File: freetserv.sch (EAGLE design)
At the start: 72 parts, among them IC2 SN75240PW, Q1 12MHz, Q2 6MHz, U1 MCP16311-E/MS

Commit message: wire up a serial port
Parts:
- removed SL1: (no value), con-lstb:MA05-1
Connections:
- removed net N$25: DRV0A.DOUT1, SL1.2
- removed net N$8: DRV0A.DOUT2, SL1.4
- new net N$37: DRV0A.DOUT1
- net GND: no longer SL1.5
- net N$19: no longer SL1.1
- net N$9: no longer SL1.3
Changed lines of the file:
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@@
 <attribute name="PARTNO" value="1276-1003-1-ND"/>
 </part>
-<part name="SL1" library="con-lstb" deviceset="MA05-1" device=""/>
 <part name="C17" library="resistor" deviceset="C-EU" device="C0805" value="0.1uF">
 <attribute name="PARTNO" value="1276-1003-1-ND"/>
@@
 <attribute name="PARTNO" value="490-10517-1-ND"/>
 </part>
-<part name="GND11" library="supply1" deviceset="GND" device=""/>
 <part name="DRV0B" library="Texas Instruments_By_element14_Batch_1" deviceset="MAX3232ECPW" device="">
 <attribute name="PARTNO" value="296-19263-1-ND"/>
@@
 <attribute name="PARTNO" value="311-27.0CRCT-ND"/>
 </part>
+<part name="GND11" library="supply1" deviceset="GND" device=""/>
+<part name="GND57" library="supply1" deviceset="GND" device=""/>
 </parts>
 <sheets>
@@
 <attribute name="PARTNO" x="134.62" y="86.36" size="1.778" layer="96" display="off"/>
 </instance>
-<instance part="SL1" gate="G$1" x="195.58" y="104.14" rot="R180"/>
 <instance part="C17" gate="G$1" x="137.16" y="114.3" rot="R90">
 <attribute name="PARTNO" x="137.16" y="114.3" size="1.778" layer="96" display="off"/>
@@
 <instance part="GND2" gate="1" x="-45.72" y="350.52"/>
 <instance part="GND3" gate="1" x="-63.5" y="322.58" rot="R90"/>
-<instance part="U$1" gate="G$1" x="-55.88" y="-73.66">
-<attribute name="PARTNO" x="-55.88" y="-73.66" size="1.778" layer="96" display="off"/>
+<instance part="U$1" gate="G$1" x="251.46" y="266.7" rot="R270">
+<attribute name="PARTNO" x="251.46" y="266.7" size="1.778" layer="96" rot="R270" display="off"/>
 </instance>
 <instance part="U1" gate="G$1" x="2.54" y="330.2">
@@
 <attribute name="PARTNO" x="66.04" y="330.2" size="1.778" layer="96" display="off"/>
 </instance>
-<instance part="GND11" gate="1" x="187.96" y="96.52"/>
 <instance part="DRV0B" gate="A" x="269.24" y="71.12">
 <attribute name="PARTNO" x="269.24" y="71.12" size="1.778" layer="96" display="off"/>
@@
 <attribute name="PARTNO" x="88.9" y="261.62" size="1.778" layer="96" display="off"/>
 </instance>
+<instance part="GND11" gate="1" x="243.84" y="129.54" rot="R270"/>
+<instance part="GND57" gate="1" x="243.84" y="127" rot="R270"/>
 </instances>
 <busses>
@@
 </segment>
 <segment>
-<pinref part="SL1" gate="G$1" pin="5"/>
-<pinref part="GND11" gate="1" pin="GND"/>
-</segment>
-<segment>
 <pinref part="DRV0B" gate="A" pin="GND"/>
 <pinref part="GND12" gate="1" pin="GND"/>
@@
 <wire x1="142.24" y1="109.22" x2="129.54" y2="109.22" width="0.1524" layer="91"/>
 <wire x1="129.54" y1="109.22" x2="129.54" y2="124.46" width="0.1524" layer="91"/>
-<wire x1="129.54" y1="124.46" x2="187.96" y2="124.46" width="0.1524" layer="91"/>
-<pinref part="SL1" gate="G$1" pin="1"/>
-<wire x1="187.96" y1="124.46" x2="187.96" y2="109.22" width="0.1524" layer="91"/>
+<wire x1="129.54" y1="124.46" x2="198.12" y2="124.46" width="0.1524" layer="91"/>
+<wire x1="198.12" y1="124.46" x2="198.12" y2="132.08" width="0.1524" layer="91"/>
+<wire x1="198.12" y1="132.08" x2="246.38" y2="132.08" width="0.1524" layer="91"/>
 </segment>
 </net>
@@
 </segment>
 </net>
-<net name="N$8" class="0">
-<segment>
-<pinref part="DRV0A" gate="A" pin="DOUT2"/>
-<wire x1="177.8" y1="104.14" x2="182.88" y2="106.68" width="0.1524" layer="91"/>
-<wire x1="182.88" y1="106.68" x2="182.88" y2="101.6" width="0.1524" layer="91"/>
-<pinref part="SL1" gate="G$1" pin="4"/>
-<wire x1="182.88" y1="101.6" x2="187.96" y2="101.6" width="0.1524" layer="91"/>
-</segment>
-</net>
 <net name="N$9" class="0">
 <segment>
@@
 <wire x1="124.46" y1="106.68" x2="116.84" y2="106.68" width="0.1524" layer="91"/>
 <wire x1="116.84" y1="106.68" x2="116.84" y2="127" width="0.1524" layer="91"/>
-<wire x1="116.84" y1="127" x2="203.2" y2="127" width="0.1524" layer="91"/>
-<wire x1="203.2" y1="127" x2="203.2" y2="88.9" width="0.1524" layer="91"/>
-<wire x1="203.2" y1="88.9" x2="177.8" y2="88.9" width="0.1524" layer="91"/>
-<wire x1="177.8" y1="88.9" x2="177.8" y2="104.14" width="0.1524" layer="91"/>
-<pinref part="SL1" gate="G$1" pin="3"/>
-<wire x1="187.96" y1="104.14" x2="177.8" y2="104.14" width="0.1524" layer="91"/>
+<wire x1="246.38" y1="137.16" x2="193.04" y2="137.16" width="0.1524" layer="91"/>
+<wire x1="193.04" y1="137.16" x2="193.04" y2="127" width="0.1524" layer="91"/>
+<wire x1="193.04" y1="127" x2="116.84" y2="127" width="0.1524" layer="91"/>
 </segment>
 </net>
@@
 <wire x1="119.38" y1="10.16" x2="119.38" y2="-20.32" width="0.1524" layer="91"/>
 <wire x1="119.38" y1="-20.32" x2="393.7" y2="-20.32" width="0.1524" layer="91"/>
-</segment>
-</net>
-<net name="N$25" class="0">
-<segment>
-<pinref part="SL1" gate="G$1" pin="2"/>
-<wire x1="187.96" y1="106.68" x2="185.42" y2="106.68" width="0.1524" layer="91"/>
-<wire x1="185.42" y1="106.68" x2="185.42" y2="109.22" width="0.1524" layer="91"/>
-<pinref part="DRV0A" gate="A" pin="DOUT1"/>
-<wire x1="185.42" y1="109.22" x2="177.8" y2="114.3" width="0.1524" layer="91"/>
 </segment>
 </net>
@@
 </segment>
 </net>
+<net name="N$8" class="0">
+<segment>
+<wire x1="246.38" y1="119.38" x2="210.82" y2="119.38" width="0.1524" layer="91"/>
+<wire x1="210.82" y1="119.38" x2="210.82" y2="104.14" width="0.1524" layer="91"/>
+<wire x1="210.82" y1="104.14" x2="177.8" y2="104.14" width="0.1524" layer="91"/>
+</segment>
+</net>
+<net name="N$37" class="0">
+<segment>
+<wire x1="246.38" y1="124.46" x2="203.2" y2="124.46" width="0.1524" layer="91"/>
+<wire x1="203.2" y1="124.46" x2="203.2" y2="114.3" width="0.1524" layer="91"/>
+<pinref part="DRV0A" gate="A" pin="DOUT1"/>
+<wire x1="203.2" y1="114.3" x2="177.8" y2="114.3" width="0.1524" layer="91"/>
+</segment>
+</net>

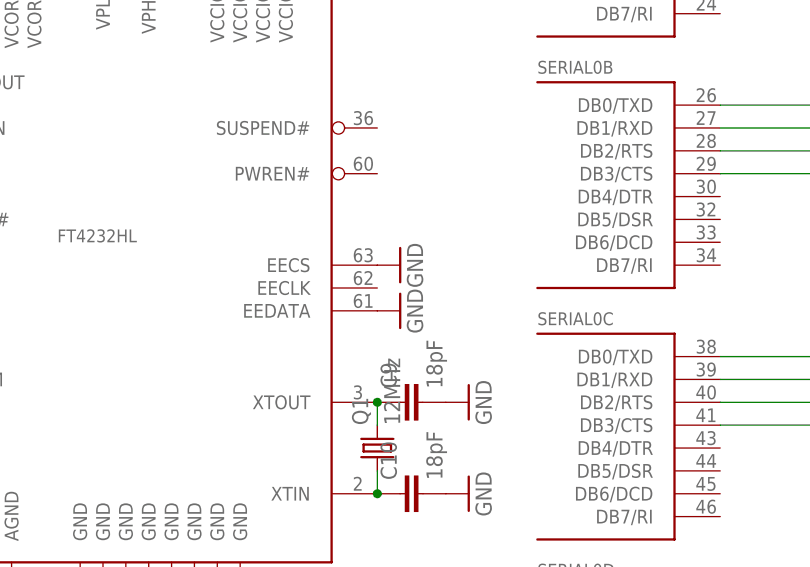
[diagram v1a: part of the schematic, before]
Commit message: Bugfix: disconnect EEDATA/EECS from GND (Thanks Volker!)
With this fix, the FTDI converter is recognized by the host \o/
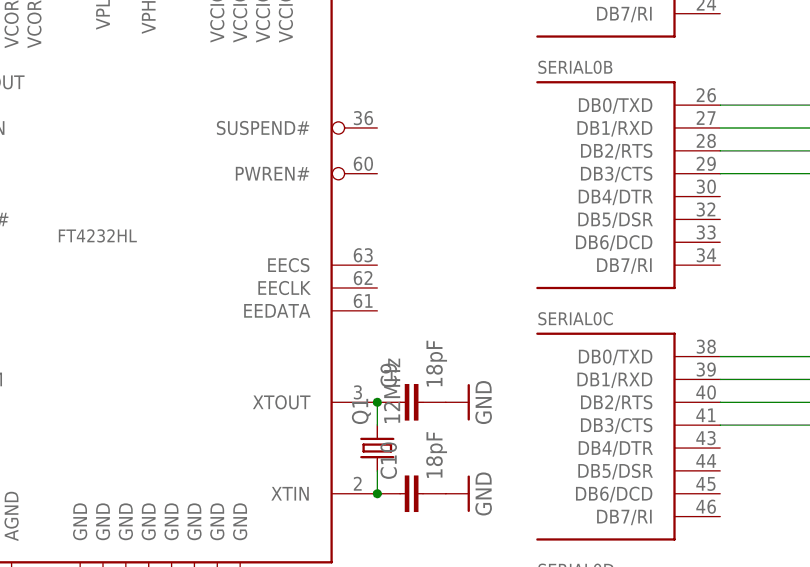
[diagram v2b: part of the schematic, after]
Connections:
- net GND: no longer SERIAL0CORE.EECS, SERIAL0CORE.EEDATA
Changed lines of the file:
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@@
 <?xml version="1.0" encoding="utf-8"?>
 <!DOCTYPE eagle SYSTEM "eagle.dtd">
-<eagle version="7.3.0">
+<eagle version="7.4.0">
 <drawing>
 <settings>
@@
 <part name="GND17" library="supply1" deviceset="GND" device=""/>
 <part name="GND18" library="supply1" deviceset="GND" device=""/>
-<part name="GND19" library="supply1" deviceset="GND" device=""/>
-<part name="GND20" library="supply1" deviceset="GND" device=""/>
 <part name="FERRITE1" library="Wurth_Elektronik_Passive_rev15d" deviceset="WE-KI" device="_0805A" value="330">
 <attribute name="PARTNO" value="490-5988-1-ND"/>
@@
 <instance part="GND17" gate="1" x="71.12" y="40.64" rot="R90"/>
 <instance part="GND18" gate="1" x="71.12" y="30.48" rot="R90"/>
-<instance part="GND19" gate="1" x="63.5" y="55.88" rot="R90"/>
-<instance part="GND20" gate="1" x="63.5" y="50.8" rot="R90"/>
 <instance part="FERRITE1" gate="G$1" x="35.56" y="116.84" rot="R270">
 <attribute name="PARTNO" x="35.56" y="116.84" size="1.778" layer="96" display="off"/>
@@
 </segment>
 <segment>
-<pinref part="SERIAL0" gate="CORE" pin="EECS"/>
-<pinref part="GND19" gate="1" pin="GND"/>
-</segment>
-<segment>
-<pinref part="SERIAL0" gate="CORE" pin="EEDATA"/>
-<pinref part="GND20" gate="1" pin="GND"/>
-</segment>
-<segment>

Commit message: Volker re-organized the schematics
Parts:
- removed DRV0A, DRV0B, DRV0C, DRV0D: MAX3232ECPW, Texas Instruments_By_element14_Batch_1:MAX3232ECPW
- removed FERRITE1, FERRITE2: 330, Wurth_Elektronik_Passive_rev15d:WE-KI_0805A
- removed HUB0: TUSB2046BVF, Texas Instruments_By_element14_Batch_1:TUSB2046BVF
- removed SERIAL0: FT4232HL, ftdichip-6:FT4232HL
- removed U1: MCP16311-E/MS, microchip:MCP16311-E/MS
- added C46: 0.1uF, resistor:C-EUC0805
- added FB1, FB2\: 330, Wurth_Elektronik_Passive_rev15d:WE-KI_0805A
- added IC1: MCP16311-E/MS, microchip:MCP16311-E/MS
- added IC3: TUSB2046BVF, Texas Instruments_By_element14_Batch_1:TUSB2046BVF
- added IC4: FT4232HL, ftdichip-6:FT4232HL
- added IC5, IC6, IC7, IC8: MAX3232ECPW, Texas Instruments_By_element14_Batch_1:MAX3232ECPW
- added R10, R9: 27, resistor:R-EU_R0805
- added R11, R12: 10k, resistor:R-EU_R0805
- added SL1, SL2, SL3, SL4: (no value), con-lstb:MA05-1
- R2: value 12K -> 12K / 1%
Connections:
- net N$12 renamed DX0_N
- net N$13 renamed DX0_P
- removed net N$19: DRV0A.RIN1
- removed net N$20: C1.1, DRV0B.C1-
- removed net N$23: DRV0B.DIN1, SERIAL0B.DB0/TXD
- removed net N$24: DRV0B.ROUT1, SERIAL0B.DB1/RXD
- removed net N$26: C23.2, DRV0B.V+
- removed net N$35: DRV0A.DIN1, SERIAL0A.DB0/TXD
- removed net N$36: DRV0A.ROUT1, SERIAL0A.DB1/RXD
- removed net N$38: C24.2, DRV0B.V-
- removed net N$41: IC2.D, R6.2, R8.2
- removed net N$43: C37.2, HUB0.~RESET, R7.1, SERIAL0CORE.RESET#
- removed net N$5: DRV0A.DIN2, SERIAL0A.DB2/RTS
- removed net N$51: C26.2, DRV0C.C1+
- removed net N$54: C27.1, DRV0C.C2-
- removed net N$55: DRV0C.DIN1, SERIAL0C.DB0/TXD
- removed net N$56: DRV0C.ROUT1, SERIAL0C.DB1/RXD
- removed net N$58: C28.2, DRV0C.V+
- removed net N$59: C29.2, DRV0C.V-
- removed net N$65: C31.2, DRV0D.C1+
- removed net N$68: C32.1, DRV0D.C2-
- removed net N$69: DRV0D.DIN1, SERIAL0D.DB0/TXD
- removed net N$7: DRV0A.ROUT2, SERIAL0A.DB3/CTS
- removed net N$70: DRV0D.ROUT1, SERIAL0D.DB1/RXD
- removed net N$72: C33.2, DRV0D.V+
- removed net N$73: C34.2, DRV0D.V-
- removed net N$75: DRV0D.DIN2, SERIAL0D.DB2/RTS
- removed net N$76: DRV0D.ROUT2, SERIAL0D.DB3/CTS
- removed net N$9: DRV0A.RIN2
- removed net USB0_D2_N: HUB0.DM2, SERIAL0CORE.USBDM
- removed net USB0_D2_P: HUB0.DP2, SERIAL0CORE.USBDP
- removed net USB0_DM_N: HUB0.DM0, IC2.C, R1.2
- removed net USB0_DM_P: HUB0.DP0, R6.1
- new net !OVRCUR1: IC3.~OVRCUR1, R11.2
- new net !OVRCUR2: IC3.~OVRCUR2, R12.2
- new net !OVRCUR3: IC3.~OVRCUR3
- new net !OVRCUR4: IC3.~OVRCUR4
- new net !PWRON1: IC3.~PWRON1
- new net !PWRON2: IC3.~PWRON2
- new net !PWRON3: IC3.~PWRON3
- new net !PWRON4: IC3.~PWRON4
- new net !RESET: C37.2, IC3.~RESET, IC4CORE.RESET#, R7.1
- new net CTS1E: IC5.RIN2, SL1.3
- new net CTS1I: IC4A.DB3/CTS, IC5.ROUT2
- new net CTS2E: IC6.RIN2, SL2.3
- new net CTS2I: IC4B.DB3/CTS, IC6.ROUT2
- new net CTS3E: IC7.RIN2, SL3.3
- new net CTS3I: IC4C.DB3/CTS, IC7.ROUT2
- new net CTS4E: IC8.RIN2, SL4.3
- new net CTS4I: IC4D.DB3/CTS, IC8.ROUT2
- new net D0_N: IC2.B, IC3.DM0, R1.2
- new net D0_P: IC2.A, IC3.DP0, R6.2, R8.2
- new net D1_N: IC2.D, IC3.DM1, R9.2
- new net D1_P: IC2.C, IC3.DP1, R10.2
- new net D2_N: IC3.DM2, IC4CORE.USBDM
- new net D2_P: IC3.DP2, IC4CORE.USBDP
- new net D3_N: IC3.DM3
- new net D3_P: IC3.DP3
- new net D4_N: IC3.DM4
- new net D4_P: IC3.DP4
- new net DX1_N: R9.1, USB_IN.D-
- new net DX1_P: R10.1, USB_IN.D+
- new net N$12: C22.1, IC6.C2-
- new net N$49: C27.1, IC7.C2-
- new net N$60: C31.2, IC8.C1+
- new net N$63: C32.1, IC8.C2-
- new net RTS1E: IC5.DOUT2, SL1.4
- new net RTS1I: IC4A.DB2/RTS, IC5.DIN2
- new net RTS2E: IC6.DOUT2, SL2.4
- new net RTS2I: IC4B.DB2/RTS, IC6.DIN2
- new net RTS3E: IC7.DOUT2, SL3.4
- new net RTS3I: IC4C.DB2/RTS, IC7.DIN2
- new net RTS4E: IC8.DOUT2, SL4.4
- new net RTS4I: IC4D.DB2/RTS, IC8.DIN2
- new net RXD1E: IC5.RIN1, SL1.1
- new net RXD1I: IC4A.DB1/RXD, IC5.ROUT1
- new net RXD2E: IC6.RIN1, SL2.1
- new net RXD2I: IC4B.DB1/RXD, IC6.ROUT1
- new net RXD3E: IC7.RIN1, SL3.1
- new net RXD3I: IC4C.DB1/RXD, IC7.ROUT1
- new net RXD4E: IC8.RIN1, SL4.1
- new net RXD4I: IC4D.DB1/RXD, IC8.ROUT1
- new net TXD1E: IC5.DOUT1, SL1.2
- new net TXD1I: IC4A.DB0/TXD, IC5.DIN1
- new net TXD2E: IC6.DOUT1, SL2.2
- new net TXD2I: IC4B.DB0/TXD, IC6.DIN1
- new net TXD3E: IC7.DOUT1, SL3.2
- new net TXD3I: IC4C.DB0/TXD, IC7.DIN1
- new net TXD4E: IC8.DOUT1, SL4.2
- new net TXD4I: IC4D.DB0/TXD, IC8.DIN1
- net +1V8: now also IC4CORE.VCORE@1, IC4CORE.VCORE@2, IC4CORE.VCORE@3, IC4CORE.VREGOUT; no longer SERIAL0CORE.VCORE@1, SERIAL0CORE.VCORE@2, SERIAL0CORE.VCORE@3, SERIAL0CORE.VREGOUT
- net +3V3: now also C46.2, FB1.1, FB2\.1, IC3.VCC, IC3.~EXTMEM, IC4CORE.VCCIO@1, IC4CORE.VCCIO@2, IC4CORE.VCCIO@3, IC4CORE.VCCIO@4, IC4CORE.VREGIN, IC5.VCC, IC6.VCC, IC7.VCC, IC8.VCC, R11.1, R12.1, R6.1; no longer DRV0A.VCC, DRV0B.VCC, DRV0C.VCC, DRV0D.VCC, FERRITE1.1, FERRITE2.1, HUB0.VCC, HUB0.VCC_2, HUB0.~EXTMEM, HUB0.~OVRCUR1, HUB0.~OVRCUR2, HUB0.~OVRCUR3, HUB0.~OVRCUR4, SERIAL0CORE.VCCIO@1, SERIAL0CORE.VCCIO@2, SERIAL0CORE.VCCIO@3, SERIAL0CORE.VCCIO@4, SERIAL0CORE.VREGIN
- net +5V: now also IC1.EN, IC1.VIN; no longer U1.EN, U1.VIN
- net GND: now also C46.1, IC1.AGND, IC1.GND, IC3.BUSPWR, IC3.GND, IC3.TSTMODE, IC3.TSTPLL/48MCLK, IC4CORE.AGND, IC4CORE.GND@1, IC4CORE.GND@2, IC4CORE.GND@3, IC4CORE.GND@4, IC4CORE.GND@5, IC4CORE.GND@6, IC4CORE.GND@7, IC4CORE.GND@8, IC4CORE.TEST, IC5.GND, IC6.GND, IC7.GND, IC8.GND, SL1.5, SL2.5, SL3.5, SL4.5; no longer DRV0A.GND, DRV0B.GND, DRV0C.GND, DRV0D.GND, HUB0.BUSPWR, HUB0.EEDATA/GANGED, HUB0.GND, HUB0.GND_2, HUB0.TSTMODE, HUB0.TSTPLL/48MCLK, SERIAL0CORE.AGND, SERIAL0CORE.GND@1, SERIAL0CORE.GND@2, SERIAL0CORE.GND@3, SERIAL0CORE.GND@4, SERIAL0CORE.GND@5, SERIAL0CORE.GND@6, SERIAL0CORE.GND@7, SERIAL0CORE.GND@8, SERIAL0CORE.TEST, U1.AGND, U1.GND
- net N$1: now also C1.2, IC6.C1+; no longer HUB0.DP1, IC2.B, USB_IN.D+
- net N$10: now also IC1.VCC; no longer U1.VCC
- net N$11: now also C22.2, IC6.C2+; no longer C1.2, DRV0B.C1+
- net N$14: now also IC4CORE.REF; no longer SERIAL0CORE.REF
- net N$15: now also IC4CORE.XTOUT; no longer SERIAL0CORE.XTOUT
- net N$16: now also IC4CORE.XTIN; no longer SERIAL0CORE.XTIN
- net N$17: now also FB2\.2, IC4CORE.VPHY; no longer FERRITE1.2, SERIAL0CORE.VPHY
- net N$18: now also FB1.2, IC4CORE.VPLL; no longer FERRITE2.2, SERIAL0CORE.VPLL
- net N$2: now also C1.1, IC6.C1-; no longer HUB0.DM1, IC2.A, USB_IN.D-
- net N$21: now also C23.2, IC6.V+; no longer C22.2, DRV0B.C2+
- net N$22: now also C24.2, IC6.V-; no longer C22.1, DRV0B.C2-
- net N$3: now also IC1.BOOST; no longer U1.BOOST
- net N$31: now also IC5.C1+; no longer DRV0A.C1+
- net N$32: now also IC5.C1-; no longer DRV0A.C1-
- net N$33: now also IC5.C2+; no longer DRV0A.C2+
- net N$34: now also IC5.C2-; no longer DRV0A.C2-
- net N$37: now also IC3.XTAL2, R3.1; no longer DRV0A.DOUT1
- net N$39: now also IC5.V+; no longer DRV0A.V+
- net N$4: now also IC1.SW; no longer U1.SW
- net N$40: now also IC5.V-; no longer DRV0A.V-
- net N$44: now also IC3.XTAL1; no longer HUB0.XTAL1
- net N$46: now also C26.2, IC7.C1+; no longer HUB0.XTAL2, R3.1
- net N$47: now also C26.1, IC7.C1-; no longer DRV0B.DIN2, SERIAL0B.DB2/RTS
- net N$48: now also C27.2, IC7.C2+; no longer DRV0B.ROUT2, SERIAL0B.DB3/CTS
- net N$52: now also C28.2, IC7.V+; no longer C26.1, DRV0C.C1-
- net N$53: now also C29.2, IC7.V-; no longer C27.2, DRV0C.C2+
- net N$6: now also IC1.VFB; no longer U1.VFB
- net N$61: now also C31.1, IC8.C1-; no longer DRV0C.DIN2, SERIAL0C.DB2/RTS
- net N$62: now also C32.2, IC8.C2+; no longer DRV0C.ROUT2, SERIAL0C.DB3/CTS
- net N$66: now also C33.2, IC8.V+; no longer C31.1, DRV0D.C1-
- net N$67: now also C34.2, IC8.V-; no longer C32.2, DRV0D.C2+
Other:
- note added: "(GPIO, SCT, ADC)"
- note added: "(I2C0)"
- note added: "(I2C1)"
- note added: "(I2C1, 3V3 analog)"
- note added: "(SSP0, 3V3 analog)"
- note added: "(with RTS/CTS support)"
- note added: "(with bootloader capability)"
- note added: "+3V3, +5V, GND"
- note added: "12MHz"
- note added: "1x DAC"
- note added: "1x I2C"
- note added: "1x SPI"
- note added: "2015/10/04"
- note added: "2015/10/05"
- note added: "2015/10/06"
- note added: "32k768Hz"
- note added: "3V3"
- note added: "3V3 Power Supply"
- note added: "3V3 analog"
- note added: "3x ADC"
- note added: "5V"
- note added: "8...24V"
- note added: "8x GPIO"
- note added: "ADC0_4 / ADC1_4"
- note added: "ADC0_5 / ADC1_5"
- note added: "ADC0_6 / ADC1_6"
- note added: "Ablage:"
- note added: "Acc & Gyro"
- note added: "Author:"
- note added: "Blockschaltbild.... (Nur als Beispiel....)"
- note added: "CAN 1"
- note added: "CAN1"
- note added: "CLK0"
- note added: "Changes:"
- note added: "Communication"
- note added: "Compass"
- note added: "Date"
- note added: "Datum"
- note added: "Debug interface"
- note added: "Developer:"
- note added: "Digital control"
- note added: "Document history:"
- note added: "Engine CH1"
- note added: "Extension"
- note added: "Freigabe Schaltplan:"
- note added: "GIT repository, https://github.com/freetserv/freetserv"
- note added: "GPIO"
- note added: "HMC5883L"
- note added: "HW -"
- note added: "HW 0.1 r0"
- note added: "I2C 0"
- note added: "I2C 1"
- note added: "I2C0"
- note added: "I2C1"
- note added: "JTAG"
- note added: "JTAG / SWD"
- note added: "Jumper"
- note added: "L6234"
- note added: "LPC4337"
- note added: "Levelshifter"
- note added: "M. Stapelberg"
- note added: "MCU"
- note added: "MPU6000"
- note added: "Oszillator"
- note added: "P1_3"
- note added: "P1_4"
- note added: "P1_5"
- note added: "P2_3"
- note added: "P2_4"
- note added: "P4_4"
- note added: "P5_0"
- note added: "P5_1"
- note added: "P5_2"
- note added: "P5_3"
- note added: "P5_4"
- note added: "P5_5"
- note added: "P5_6"
- note added: "P5_7"
- note added: "POWER IN"
- note added: "POWER OUT"
- note added: "PWM / PPM input"
- note added: "PWM outputs"
- note added: "Port"
- note added: "Power Connectors"
- note added: "PowerSupply"
- note added: "Projekt:"
- note added: "QUAD-USB-Serial Converter"
- note added: "Reset"
- note added: "Review A Schaltplan:"
- note added: "Review B Schaltplan:"
- note added: "Revisoin:"
- note added: "SSP0"
- note added: "Stand:"
- note added: "Starting from scratch"
- note added: "Status LED's"
- note added: "Switches"
- note added: "System overview"
- note added: "UART 0"
- note added: "UART 1"
- note added: "UART0"
- note added: "UART1"
- note added: "USB 0"
- note added: "USB-Chaining-Port"
- note added: "USB-Host"
- note added: "USB-Hub"
- note added: "USB-IN / OUT"
- note added: "USB0"
- note added: "Unterschrift"
- note added: "V. Wunsch"
- note added: "Version:"
- note added: "XTAL"
- note added: "do layout"
- note added: "extension"
- note added: "freetServ"
- note added: "made some changes on circuit"
- note added: "rework of schematic"
- note added: "xxx. xxxxxxx"
- note added: "xxx.xxxxxxx"

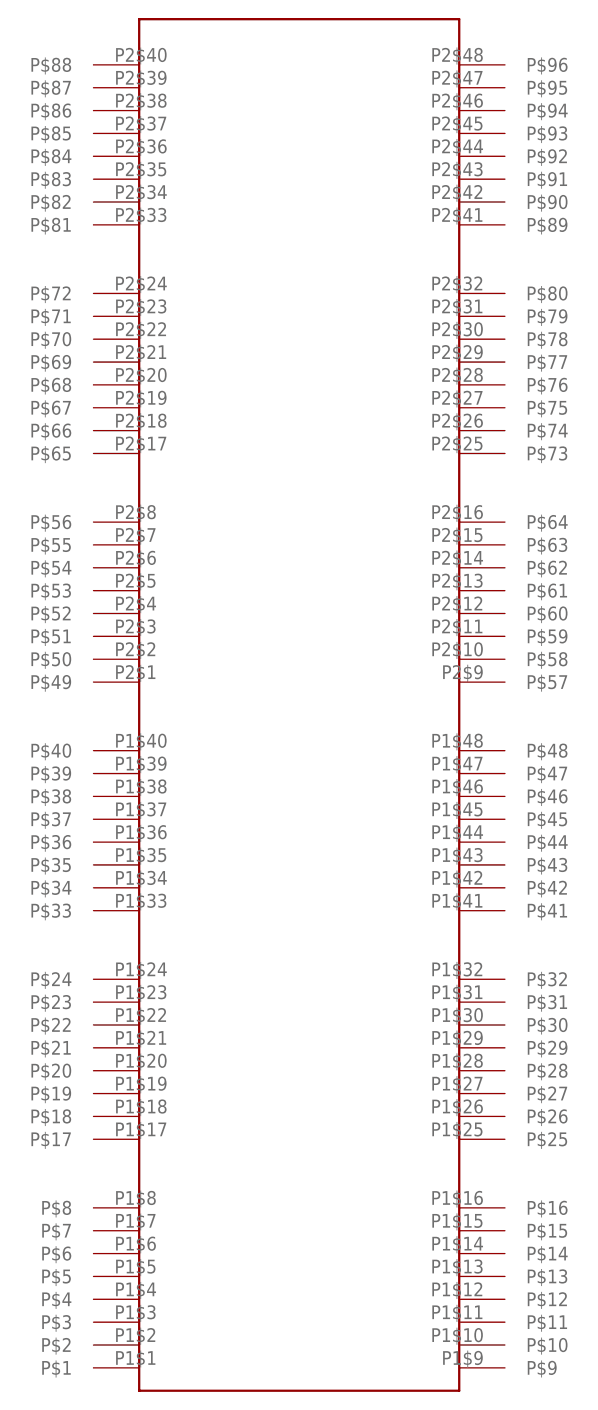
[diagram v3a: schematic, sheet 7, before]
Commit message: Volker re-routed the FTDI (work-in-progress)
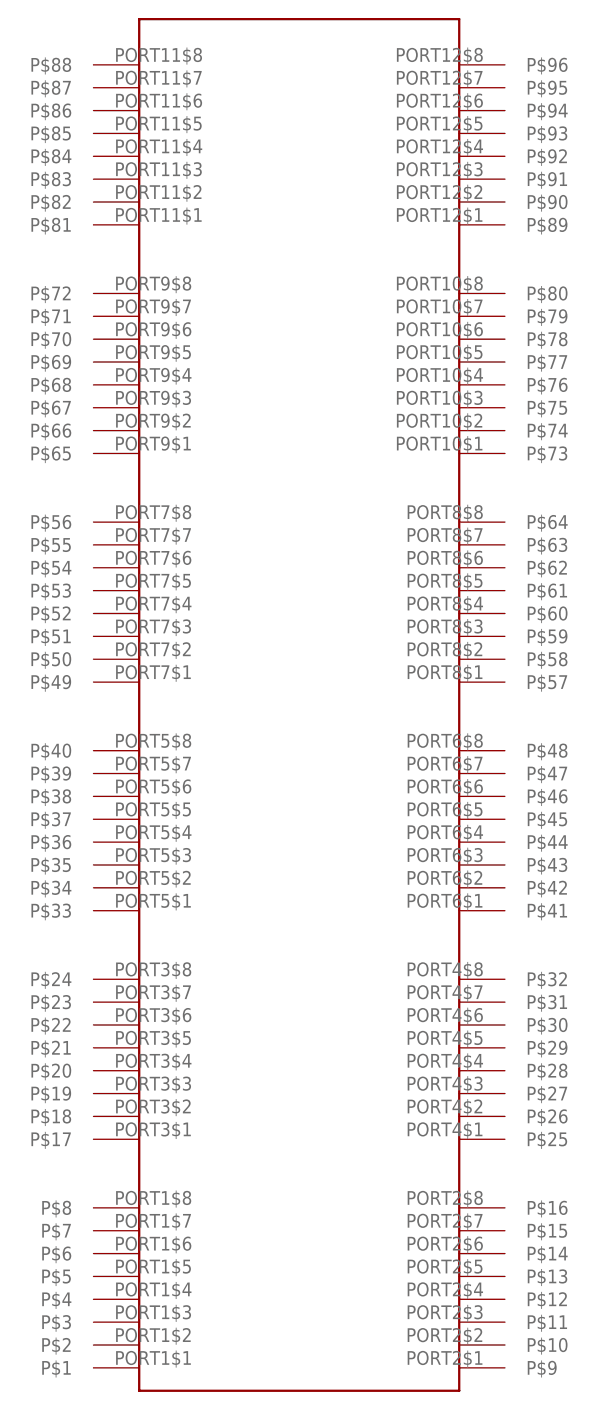
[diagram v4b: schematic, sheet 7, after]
